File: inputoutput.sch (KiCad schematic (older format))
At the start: 20 parts, among them J2 TimerCounter, J3 GPIO1, J4 GPIO2, J5 Mini-DIN-6, J6 RS232 (TTL Level), J7 CompactFlash Port, Q1 2N3904, Q2 2N3904, U11 Z84C30-CTC, U12 Z84C40-SIO-0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

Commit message: Fixed up issues
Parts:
- J5: value Mini-DIN-6 -> PS/2 Keyboard
- J6: value RS232 (TTL Level) -> RS232
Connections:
- net RXD: now reaches J6.1 (Pin_1), U12.12 (RxDA)
- net TXD: now reaches J6.2 (Pin_2), U12.15 (TxDA)
- net ~DTR: now reaches J6.5 (Pin_5), U12.16 (~DTRA)
- net ~RTS: now reaches J6.3 (Pin_3), U12.17 (~RTSA)
- net ~CTS: now reaches J6.4 (Pin_4), U12.18 (~CTSA)
- net ~DCD: now reaches J6.6 (Pin_6), U12.19 (~DCDA)
- net RxTxCLK renamed RxTxCA
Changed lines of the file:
@@
 P 10600 2800
 F 0 "J5" H 10600 3167 50  0000 C CNN
-F 1 "Mini-DIN-6" H 10600 3076 50  0000 C CNN
+F 1 "PS/2 Keyboard" H 10600 3076 50  0000 C CNN
 F 2 "Personal:Mini_din6" H 10600 2800 50  0001 C CNN
 F 3 "http://service.powerdynamics.com/ec/Catalog17/Section%2011.pdf" H 10600 2800 50  0001 C CNN
@@
 Wire Wire Line
 	1500 3150 2100 3150
-$Comp
-L Connector:Conn_01x07_Male J6
-U 1 1 60B7F4D8
-P 7900 1650
-F 0 "J6" H 7872 1674 50  0000 R CNN
-F 1 "RS232 (TTL Level)" H 8250 2050 50  0000 R CNN
-F 2 "Connector_PinHeader_2.54mm:PinHeader_1x07_P2.54mm_Vertical" H 7900 1650 50  0001 C CNN
-F 3 "~" H 7900 1650 50  0001 C CNN
-	1    7900 1650
-	-1   0    0    -1
-$EndComp
 Wire Wire Line
 	6250 1700 7250 1700
@@
 Wire Wire Line
 	9750 5050 10100 5050
+$Comp
+L power:GND #PWR0135
+U 1 1 60E1E285
+P 8000 6000
+F 0 "#PWR0135" H 8000 5750 50  0001 C CNN
+F 1 "GND" H 8005 5827 50  0000 C CNN
+F 2 "" H 8000 6000 50  0001 C CNN
+F 3 "" H 8000 6000 50  0001 C CNN
+	1    8000 6000
+	1    0    0    -1
+$EndComp
 Wire Bus Line
 	2200 7050 2200 7250
@@
 Wire Bus Line
 	1800 1050 1800 2250
-$Comp
-L power:GND #PWR0135
-U 1 1 60E1E285
-P 8000 6000
-F 0 "#PWR0135" H 8000 5750 50  0001 C CNN
-F 1 "GND" H 8005 5827 50  0000 C CNN
-F 2 "" H 8000 6000 50  0001 C CNN
-F 3 "" H 8000 6000 50  0001 C CNN
-	1    8000 6000
-	1    0    0    -1
+Text Label 7550 1350 0    50   ~ 0
+RXD
+Text Label 6450 1800 0    50   ~ 0
+RxTxCA
+Text Label 7550 1450 0    50   ~ 0
+TXD
+Text Label 7550 1550 0    50   ~ 0
+~RTS
+Text Label 7550 1650 0    50   ~ 0
+~CTS
+Text Label 7550 1750 0    50   ~ 0
+~DTR
+Text Label 7550 1850 0    50   ~ 0
+~DCD
+$Comp
+L Connector:Conn_01x07_Male J6
+U 1 1 60B7F4D8
+P 7900 1650
+F 0 "J6" H 7872 1674 50  0000 R CNN
+F 1 "RS232" H 7950 2050 50  0000 R CNN
+F 2 "Connector_PinHeader_2.54mm:PinHeader_1x07_P2.54mm_Vertical" H 7900 1650 50  0001 C CNN
+F 3 "~" H 7900 1650 50  0001 C CNN
+	1    7900 1650
+	-1   0    0    -1
 $EndComp
 $EndSCHEMATC

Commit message: Added two pullups to SIO/SYNC
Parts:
- added R30, R31: 10k, Resistor_THT:R_Axial_DIN0207_L6.3mm_D2.5mm_P10.16mm_Horizontal, symbol Device:R
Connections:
- net +5V: now also R30.1, R31.1
- net at U12.11 (~SYNCA): now also R30.2
- net at U12.29 (~SYNCB): now also R31.2
- no-connect marks 26 -> 24
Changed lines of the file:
@@
 	4700 2950 5150 2950
-Wire Wire Line
-	6250 1800 6950 1800
 Wire Wire Line
 	6250 2000 6950 2000
@@
 	1    0    0    -1
 $EndComp
-NoConn ~ 6250 2100
 NoConn ~ 6250 2200
-NoConn ~ 6250 3100
 NoConn ~ 6250 3200
 $Comp
@@
 	-1   0    0    -1
 $EndComp
+$Comp
+L Device:R R31
+U 1 1 605A697E
+P 6750 1450
+F 0 "R31" H 6820 1496 50  0000 L CNN
+F 1 "10k" H 6820 1405 50  0000 L CNN
+F 2 "Resistor_THT:R_Axial_DIN0207_L6.3mm_D2.5mm_P10.16mm_Horizontal" V 6680 1450 50  0001 C CNN
+F 3 "~" H 6750 1450 50  0001 C CNN
+	1    6750 1450
+	1    0    0    -1
+$EndComp
+Wire Wire Line
+	5950 1300 5950 1450
+Wire Wire Line
+	5950 1450 5700 1450
+Connection ~ 5700 1450
+Wire Wire Line
+	6750 1600 6750 2350
+Wire Wire Line
+	6750 2350 6700 2350
+Wire Wire Line
+	6700 2350 6700 2850
+Wire Wire Line
+	6700 2850 6650 2850
+Wire Wire Line
+	6650 2850 6650 3100
+Wire Wire Line
+	6650 3100 6250 3100
+Wire Wire Line
+	6250 2050 6250 2100
+Wire Wire Line
+	6250 1800 6950 1800
+Wire Wire Line
+	6500 2050 6250 2050
+Wire Bus Line
+	9150 4800 9400 4800
+Wire Bus Line
+	6700 4950 7700 4950
 Wire Bus Line
 	2200 7050 2200 7250
 Wire Bus Line
+	2150 5000 2150 5850
+Wire Bus Line
 	1300 2700 1300 3250
 Wire Bus Line
 	4800 3600 4800 4250
 Wire Bus Line
-	9150 4800 9400 4800
-Wire Bus Line
-	6700 4950 7700 4950
-Wire Bus Line
-	2150 5000 2150 5850
-Wire Bus Line
 	4850 1050 4850 2300
 Wire Bus Line
 	1800 1050 1800 2250
+Wire Wire Line
+	6500 1600 6500 2050
+Wire Wire Line
+	6500 1300 6750 1300
+Connection ~ 6500 1300
+Wire Wire Line
+	6500 1300 5950 1300
+$Comp
+L Device:R R30
+U 1 1 605A7BCC
+P 6500 1450
+F 0 "R30" H 6570 1496 50  0000 L CNN
+F 1 "10k" H 6570 1405 50  0000 L CNN
+F 2 "Resistor_THT:R_Axial_DIN0207_L6.3mm_D2.5mm_P10.16mm_Horizontal" V 6430 1450 50  0001 C CNN
+F 3 "~" H 6500 1450 50  0001 C CNN
+	1    6500 1450
+	1    0    0    -1
+$EndComp
 $EndSCHEMATC

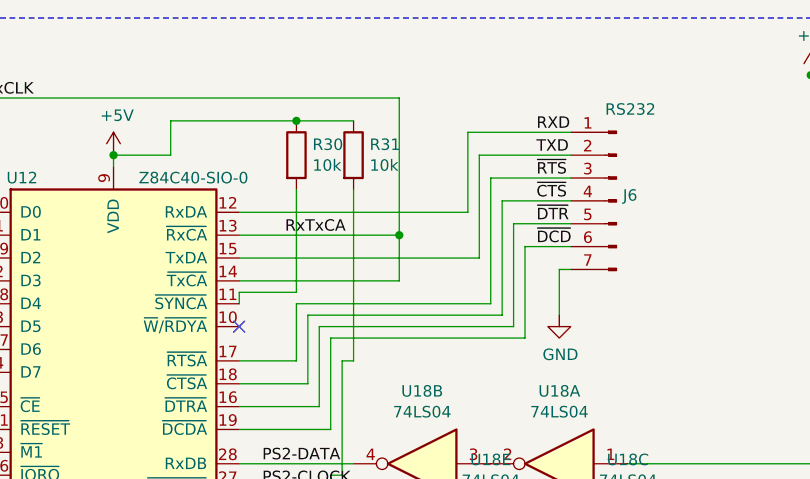
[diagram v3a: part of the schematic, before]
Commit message: Revision 2 bug fix. NMI / INT reversed. Added resistors to UART Rx/Tx
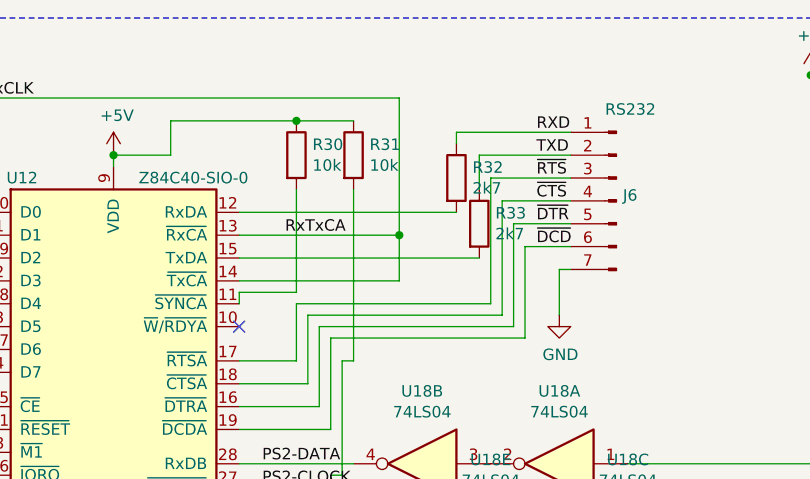
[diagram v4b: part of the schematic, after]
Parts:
- added R32, R33: 2k7, Resistor_THT:R_Axial_DIN0207_L6.3mm_D2.5mm_P10.16mm_Horizontal, symbol Device:R
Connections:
- net RXD: now also R32.1; no longer U12.12 (RxDA)
- net TXD: now also R33.1; no longer U12.15 (TxDA)
- new net: R32.2, U12.12 (RxDA)
- new net: R33.2, U12.15 (TxDA)
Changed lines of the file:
@@
 	1500 3150 2100 3150
 Wire Wire Line
-	6250 1700 7250 1700
-Wire Wire Line
-	7250 1700 7250 1350
-Wire Wire Line
-	7250 1350 7700 1350
+	6250 1700 7200 1700
 Wire Wire Line
 	7300 1450 7700 1450
-Wire Wire Line
-	7300 1450 7300 1900
 Wire Wire Line
 	7700 1950 7650 1950
@@
 Wire Wire Line
 	6500 2050 6250 2050
-Wire Bus Line
-	9150 4800 9400 4800
-Wire Bus Line
-	6700 4950 7700 4950
-Wire Bus Line
-	2200 7050 2200 7250
-Wire Bus Line
-	2150 5000 2150 5850
-Wire Bus Line
-	1300 2700 1300 3250
-Wire Bus Line
-	4800 3600 4800 4250
-Wire Bus Line
-	4850 1050 4850 2300
-Wire Bus Line
-	1800 1050 1800 2250
 Wire Wire Line
 	6500 1600 6500 2050
@@
 	1    0    0    -1
 $EndComp
+$Comp
+L Device:R R32
+U 1 1 6077BB71
+P 7200 1550
+F 0 "R32" H 7270 1596 50  0000 L CNN
+F 1 "2k7" H 7270 1505 50  0000 L CNN
+F 2 "Resistor_THT:R_Axial_DIN0207_L6.3mm_D2.5mm_P10.16mm_Horizontal" V 7130 1550 50  0001 C CNN
+F 3 "~" H 7200 1550 50  0001 C CNN
+	1    7200 1550
+	1    0    0    -1
+$EndComp
+Wire Wire Line
+	7200 1400 7200 1350
+Wire Wire Line
+	7200 1350 7700 1350
+$Comp
+L Device:R R33
+U 1 1 60791876
+P 7300 1750
+F 0 "R33" H 7370 1796 50  0000 L CNN
+F 1 "2k7" H 7370 1705 50  0000 L CNN
+F 2 "Resistor_THT:R_Axial_DIN0207_L6.3mm_D2.5mm_P10.16mm_Horizontal" V 7230 1750 50  0001 C CNN
+F 3 "~" H 7300 1750 50  0001 C CNN
+	1    7300 1750
+	1    0    0    -1
+$EndComp
+Wire Wire Line
+	7300 1600 7300 1450
+Wire Bus Line
+	2200 7050 2200 7250
+Wire Bus Line
+	1300 2700 1300 3250
+Wire Bus Line
+	4800 3600 4800 4250
+Wire Bus Line
+	9150 4800 9400 4800
+Wire Bus Line
+	6700 4950 7700 4950
+Wire Bus Line
+	2150 5000 2150 5850
+Wire Bus Line
+	4850 1050 4850 2300
+Wire Bus Line
+	1800 1050 1800 2250
 $EndSCHEMATC
